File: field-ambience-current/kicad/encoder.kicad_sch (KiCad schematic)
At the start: 24 parts

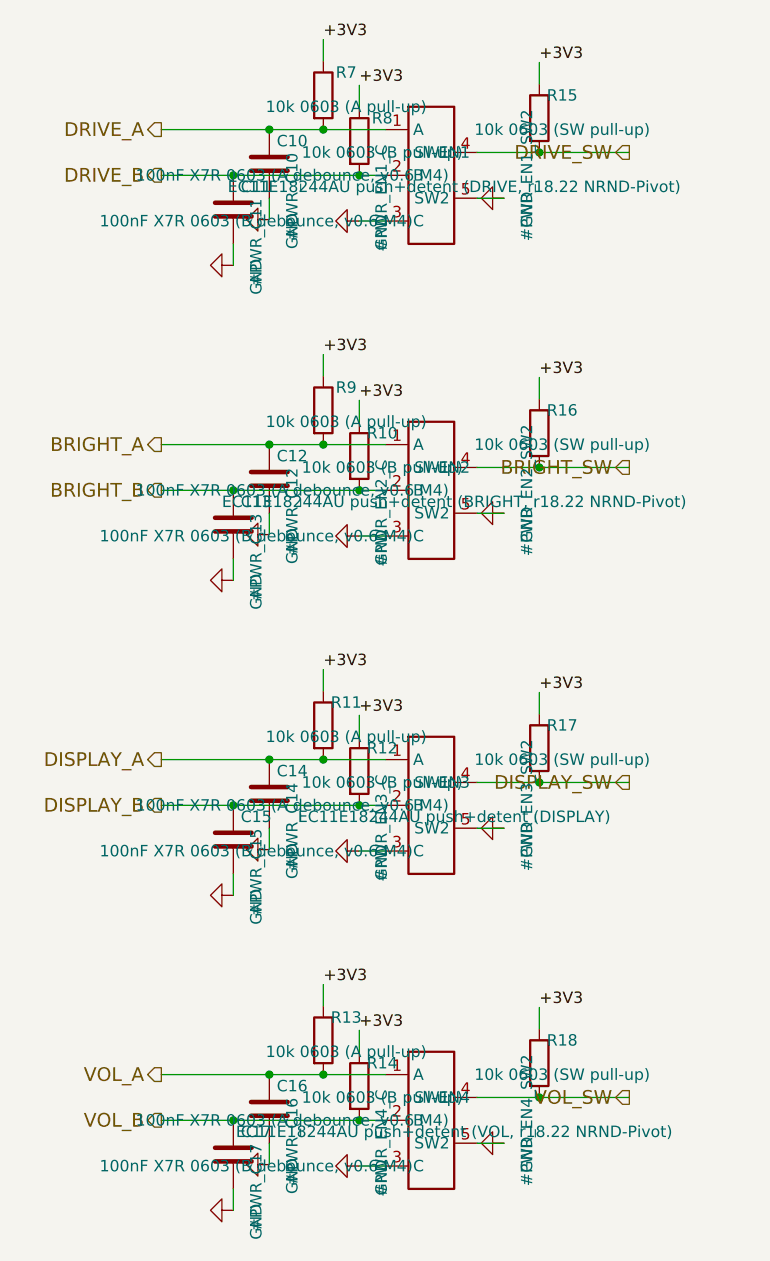
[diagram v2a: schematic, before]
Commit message: fix(pcb): datasheet verification of all remaining parts — encoder + jack pad maps were dead/wrong (r18.82) (#94)
User asked to verify all other components against datasheets. Every
remaining IC and every symbol-pin<->footprint-pad pairing was checked
against the official documents (Microchip DS20001952 + DS20001984, NXP
PCA9685 Rev 4, ST USBLC6-2 + DS12110 Fig 5, Abracon via LCSC, SHOU HAN
PJ-320D, HX B3F-4055, KiCad footprint sources).

Critical pad-mapping bugs (KiCad matches pin number to pad name as a
STRING):

1. All 4 rotary encoders were completely unconnected: the official KiCad
   footprint RotaryEncoder_Alps_EC11E-Switch_Vertical_H20mm uses NAMED
   pads A/B/C/S1/S2, the custom symbol used numeric pins 1-5 - not a
   single encoder pin would have joined a pad in the netlist. Symbol pin
   numbers renamed to the pad names (footprint geometry verified from
   the KiCad GitLab source: A(0,0), C(0,2.5) = middle common, B(0,5) =
   ALPS A-C-B terminal order).

2. PJ-320D jacks (J8 line-out, J10 MIDI): pad map was wrong. The SHOU HAN
   drawing (PCB layout + schematic) assigns pad 1=A=sleeve, 2=D=ring,
   3=C=tip-switch(detect), 4=B=tip. The symbol mapped T=1/R=2/S=3/DET=4,
   which put LEFT AUDIO on the grounded sleeve barrel, GND on the detect
   contact and JACK_DETECT on the tip. Corrected to T=4/R=2/S=1/DET=3.
   Vendored footprint geometry matches the drawing exactly (3.0/4.0mm
   pad pitch, 1.0mm locators at 7.0mm) - closes TODO B0b.

3. Consequence of the true detect topology (detect rests on the TIP when
   unplugged, i.e. on the DAC L output at +-3Vpk): added R_DET_J8 10k
   (limits MCP input-clamp current to <300uA - unprotected it would have
   clamped negative half-waves through 22R at >100mA, distorting the
   speaker feed) and C_DET_J8 1uF (filters audio AC off GPA6, fc ~16Hz).
   Levels: unplugged ~0.3V LOW, plugged 3.3V HIGH.

Datasheet-required gaps:

4. MCP73831 was missing the 4.7uF VDD input capacitor from the DS typical
   application - the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
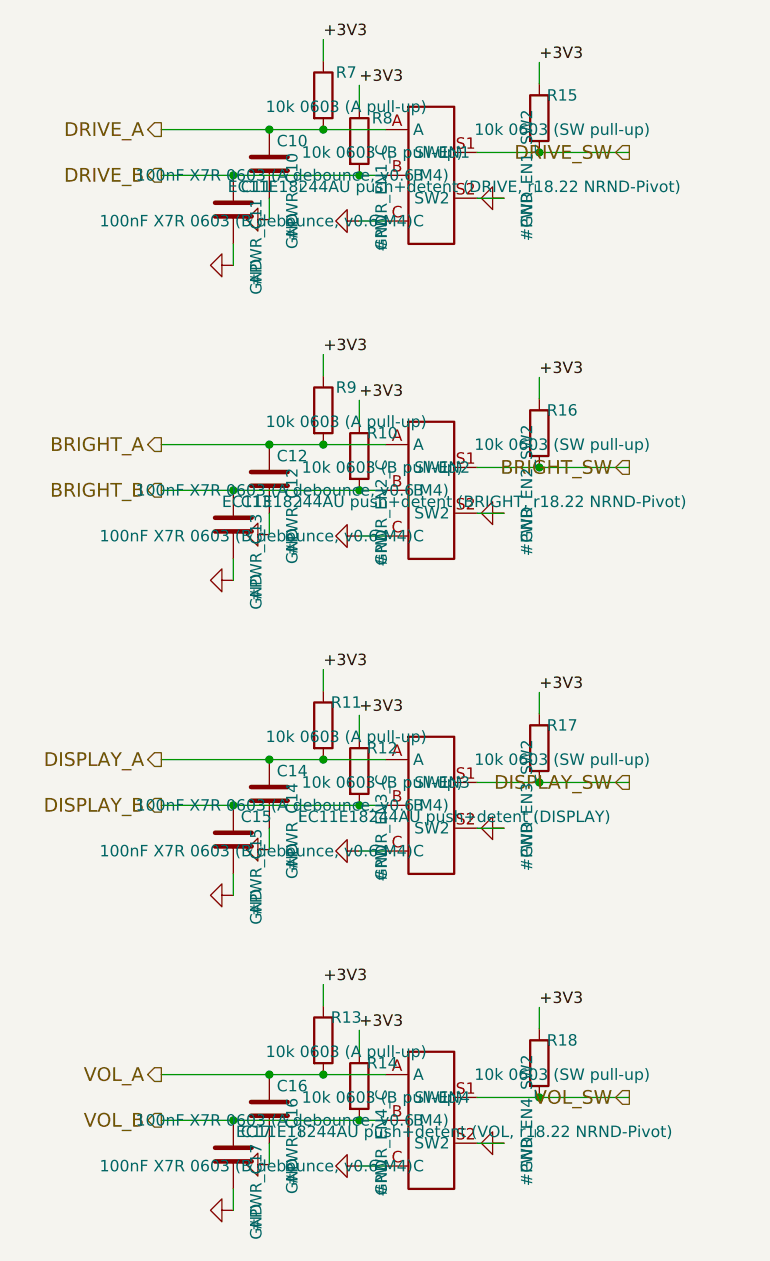
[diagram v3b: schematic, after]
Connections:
- net BRIGHT_A: now also EN2.A; no longer EN2.1 (A)
- net BRIGHT_B: now also EN2.B; no longer EN2.2 (B)
- net BRIGHT_SW: now also EN2.S1 (SW1); no longer EN2.4 (SW1)
- net DISPLAY_A: now also EN3.A; no longer EN3.1 (A)
- net DISPLAY_B: now also EN3.B; no longer EN3.2 (B)
- net DISPLAY_SW: now also EN3.S1 (SW1); no longer EN3.4 (SW1)
- net DRIVE_A: now also EN1.A; no longer EN1.1 (A)
- net DRIVE_B: now also EN1.B; no longer EN1.2 (B)
- net DRIVE_SW: now also EN1.S1 (SW1); no longer EN1.4 (SW1)
- net GND: now also EN1.C, EN1.S2 (SW2), EN2.C, EN2.S2 (SW2), EN3.C, EN3.S2 (SW2), EN4.C, EN4.S2 (SW2); no longer EN1.3 (C), EN1.5 (SW2), EN2.3 (C), EN2.5 (SW2), EN3.3 (C), EN3.5 (SW2), EN4.3 (C), EN4.5 (SW2)
- net VOL_A: now also EN4.A; no longer EN4.1 (A)
- net VOL_B: now also EN4.B; no longer EN4.2 (B)
- net VOL_SW: now also EN4.S1 (SW1); no longer EN4.4 (SW1)
